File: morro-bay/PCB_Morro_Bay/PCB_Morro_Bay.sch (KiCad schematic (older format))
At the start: 84 parts, among them J1 POWER, J2 CAN, J23 POWER_OUT, J36 SWD, J37 GPIO, J38 USB_B, J39 ESERCOM, SW3 RESET, U1 MCP2515-xSO, U13 V7805-2000R, U2 SN65HVD232, U3 AZ1117-3.3, U4 ATSAMD21J18A-AU, Y1 8MHz, Y2 30MHz, Y3 32.768kHz

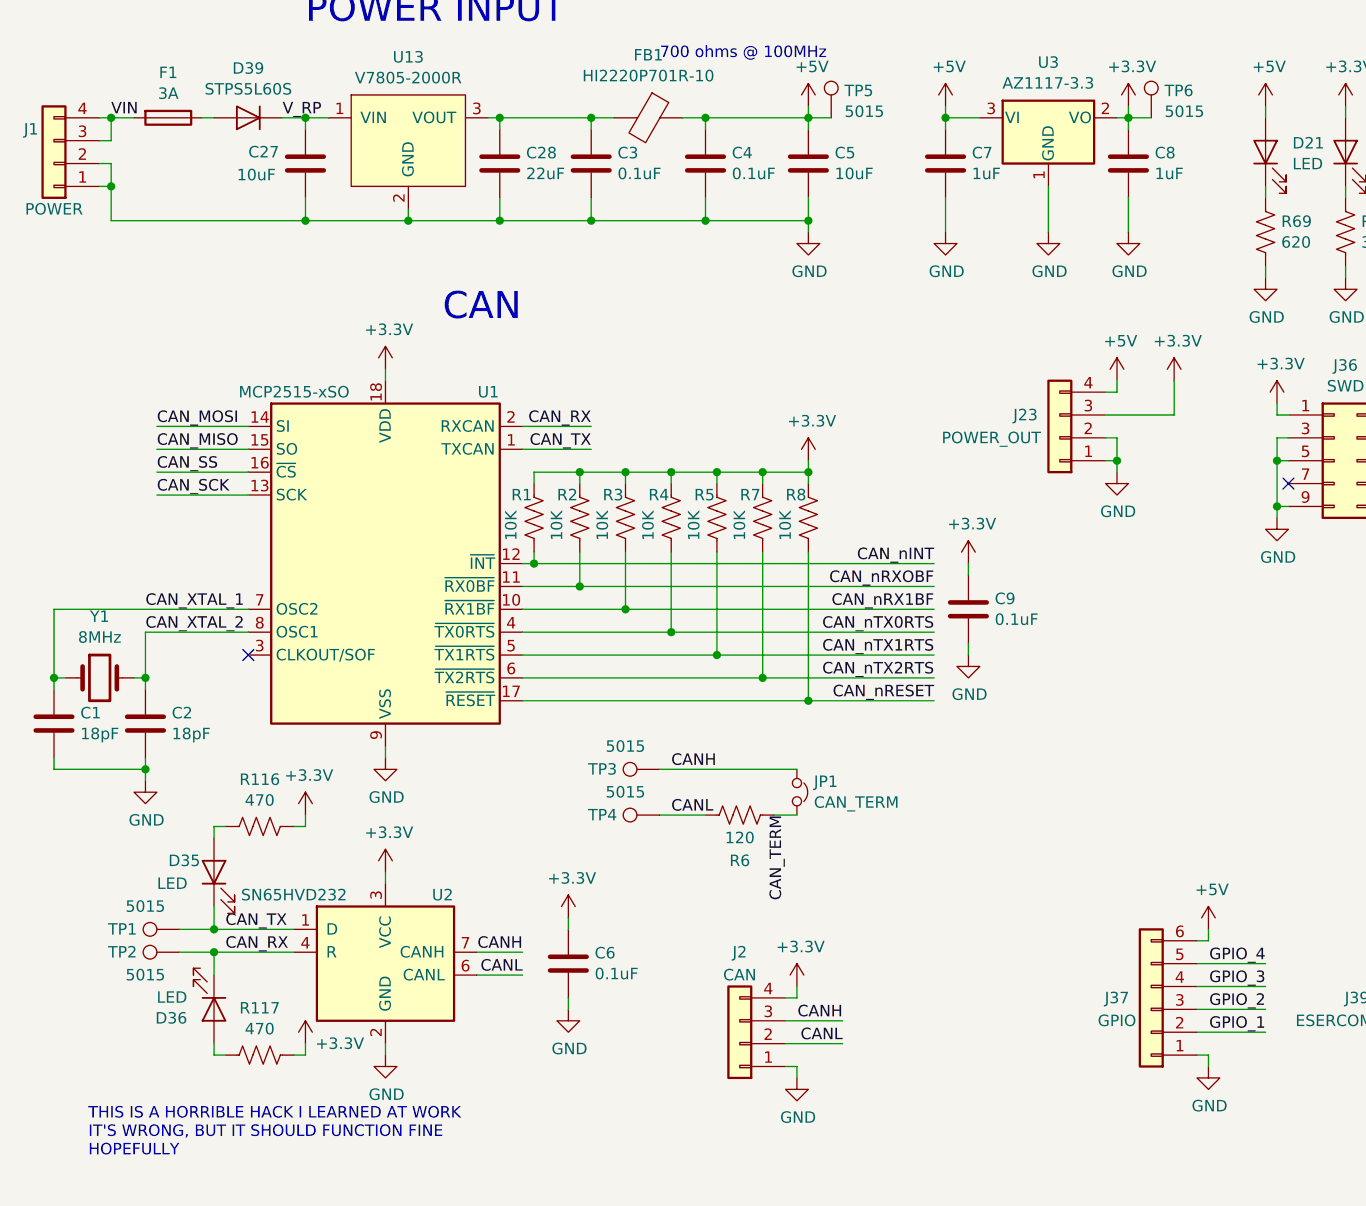
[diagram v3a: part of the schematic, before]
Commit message: Fix values of C7 and C8
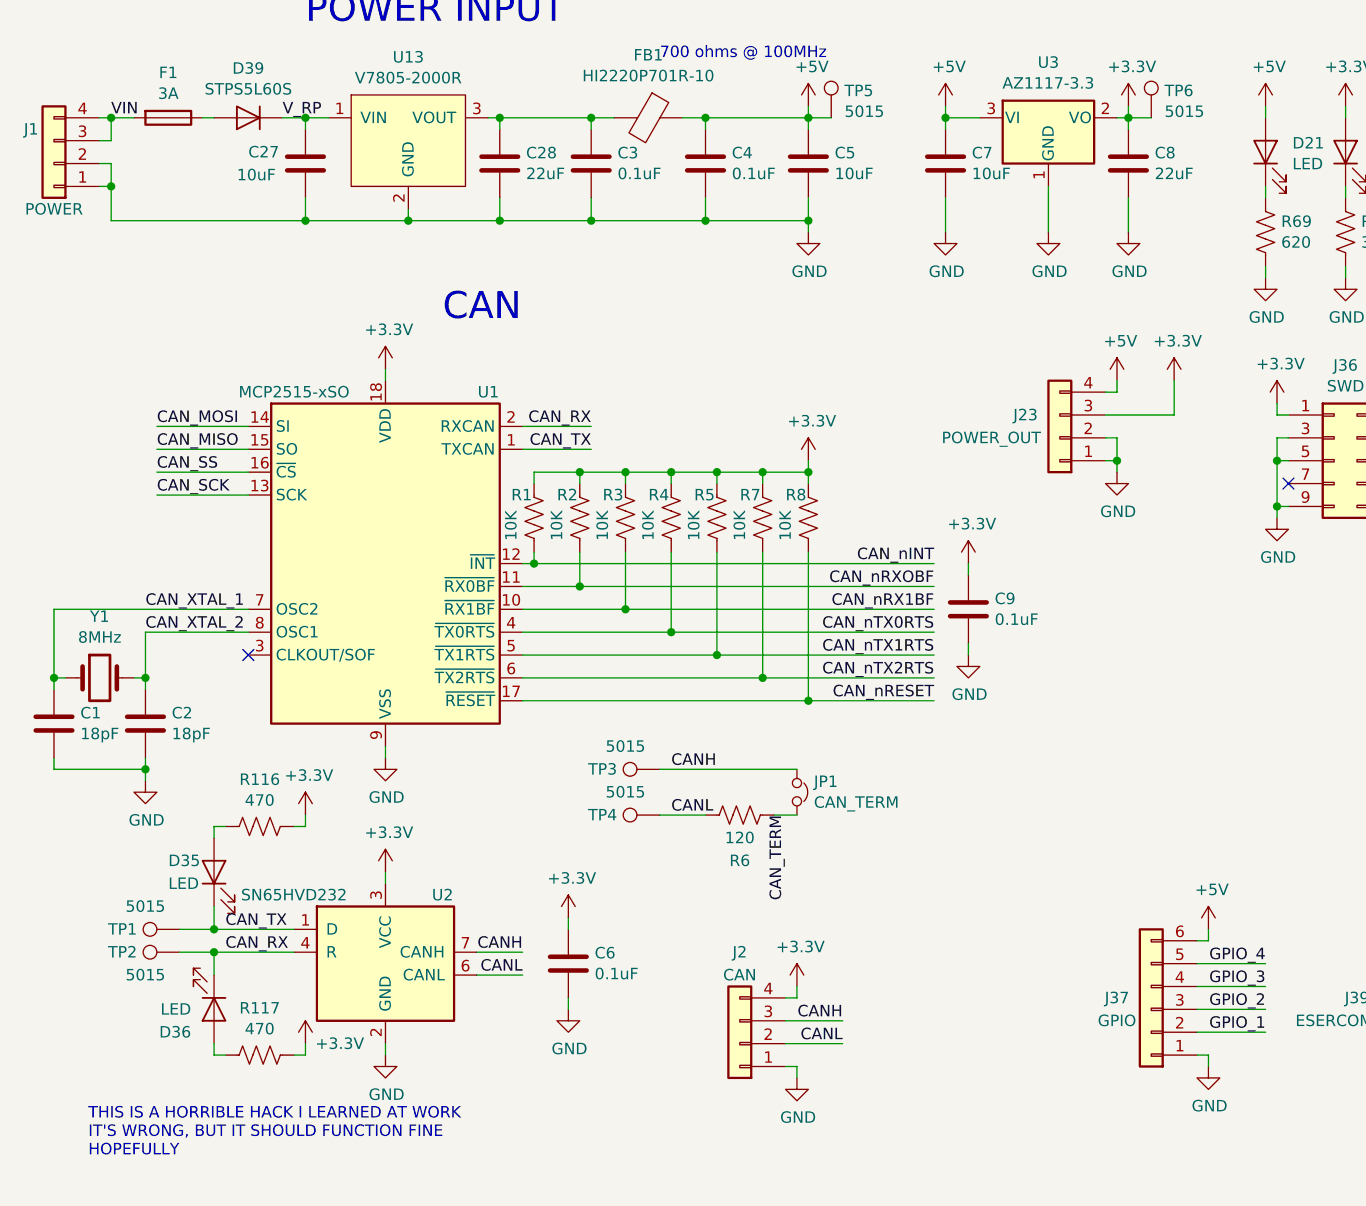
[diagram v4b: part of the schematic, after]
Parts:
- C7: value 1uF -> 10uF; Digikey https://www.digikey.ca/en/products/detail/samsung-electro-mechanics/CL10B105KA8NNNC/3886842 -> https://www.digikey.ca/en/products/detail/samsung-electro-mechanics/CL10A106MA8NRNC/3887527; Part Number CL10B105KA8NNNC -> CL10A106MA8NRNC
- C8: value 1uF -> 22uF; footprint Capacitor_SMD:C_0603_1608Metric_Pad1.05x0.95mm_HandSolder -> Capacitor_SMD:C_0805_2012Metric_Pad1.15x1.40mm_HandSolder; Digikey https://www.digikey.ca/en/products/detail/samsung-electro-m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 -> https://www.digikey.ca/product-detail/en/samsung-electro-me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; Part Number CL10B105KA8NNNC -> CL21A226MAQNNNE
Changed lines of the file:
@@
-$EndComp
-$Comp
-L Device:C C7
-U 1 1 5E3CE794
-P 4550 1350
-F 0 "C7" H 4665 1396 50  0000 L CNN
-F 1 "1uF" H 4665 1305 50  0000 L CNN
-F 2 "Capacitor_SMD:C_0603_1608Metric_Pad1.05x0.95mm_HandSolder" H 4588 1200 50  0001 C CNN
-F 3 "~" H 4550 1350 50  0001 C CNN
-F 4 "https://www.digikey.ca/en/products/detail/samsung-electro-mechanics/CL10B105KA8NNNC/3886842" H 4550 1350 50  0001 C CNN "Digikey"
-F 5 "CL10B105KA8NNNC" H 4550 1350 50  0001 C CNN "Part Number"
-	1    4550 1350
-	1    0    0    -1
 $EndComp
 $Comp
@@
 U 1 1 5ED157D8
 P 1350 5050
-F 0 "D36" V 1389 4933 50  0000 R CNN
-F 1 "LED" V 1298 4933 50  0000 R CNN
+F 0 "D36" V 1450 4950 50  0000 R CNN
+F 1 "LED" V 1350 4950 50  0000 R CNN
 F 2 "LED_SMD:LED_0603_1608Metric_Castellated" H 1350 5050 50  0001 C CNN
 F 3 "http://optoelectronics.liteon.com/upload/download/DS22-2000-222/LTST-C191KFKT.pdf" H 1350 5050 50  0001 C CNN
@@
 P 1350 4450
 F 0 "D35" V 1400 4650 50  0000 R CNN
-F 1 "LED" V 1300 4700 50  0000 R CNN
+F 1 "LED" V 1300 4650 50  0000 R CNN
 F 2 "LED_SMD:LED_0603_1608Metric_Castellated" H 1350 4450 50  0001 C CNN
 F 3 "http://optoelectronics.liteon.com/upload/download/DS22-2000-222/LTST-C191KFKT.pdf" H 1350 4450 50  0001 C CNN
@@
 $EndComp
 $Comp
-L Device:C C8
-U 1 1 5E7F39FA
-P 5350 1350
-F 0 "C8" H 5465 1396 50  0000 L CNN
-F 1 "1uF" H 5465 1305 50  0000 L CNN
-F 2 "Capacitor_SMD:C_0603_1608Metric_Pad1.05x0.95mm_HandSolder" H 5388 1200 50  0001 C CNN
-F 3 "~" H 5350 1350 50  0001 C CNN
-F 4 "https://www.digikey.ca/en/products/detail/samsung-electro-mechanics/CL10B105KA8NNNC/3886842" H 5350 1350 50  0001 C CNN "Digikey"
-F 5 "CL10B105KA8NNNC" H 5350 1350 50  0001 C CNN "Part Number"
-	1    5350 1350
-	1    0    0    -1
-$EndComp
-$Comp
 L Device:C C19
 U 1 1 5E80BB1C
@@
 	1    0    0    -1
 $EndComp
+$Comp
+L Device:C C7
+U 1 1 5E85940A
+P 4550 1350
+F 0 "C7" H 4665 1396 50  0000 L CNN
+F 1 "10uF" H 4665 1305 50  0000 L CNN
+F 2 "Capacitor_SMD:C_0603_1608Metric_Pad1.05x0.95mm_HandSolder" H 4588 1200 50  0001 C CNN
+F 3 "~" H 4550 1350 50  0001 C CNN
+F 4 "https://www.digikey.ca/en/products/detail/samsung-electro-mechanics/CL10A106MA8NRNC/3887527" H 4550 1350 50  0001 C CNN "Digikey"
+F 5 "CL10A106MA8NRNC	" H 4550 1350 50  0001 C CNN "Part Number"
+	1    4550 1350
+	1    0    0    -1
+$EndComp
+$Comp
+L Device:C C8
+U 1 1 5E88C625
+P 5350 1350
+AR Path="/5E88C625" Ref="C8"  Part="1"
+AR Path="/5E59A680/5E88C625" Ref="C?"  Part="1"
+F 0 "C8" H 5465 1396 50  0000 L CNN
+F 1 "22uF" H 5465 1305 50  0000 L CNN
+F 2 "Capacitor_SMD:C_0805_2012Metric_Pad1.15x1.40mm_HandSolder" H 5388 1200 50  0001 C CNN
+F 3 "~" H 5350 1350 50  0001 C CNN
+F 4 "CL21A226MAQNNNE" H 5350 1350 50  0001 C CNN "Part Number"
+F 5 "https://www.digikey.ca/product-detail/en/samsung-electro-mechanics/CL21A226MAQNNNE/1276-2908-1-ND/3890994" H 5350 1350 50  0001 C CNN "Digikey"
+	1    5350 1350
+	1    0    0    -1
+$EndComp

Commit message: Routing and layout work
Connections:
- net SAMD_ADC_1: now also U4.20 (PA11); no longer U4.61 (PB00)
- net SAMD_ADC_10: now also U4.11 (PB08); no longer U4.10 (PB07)
- net SAMD_ADC_11: now also U4.10 (PB07); no longer U4.11 (PB08)
- net SAMD_ADC_12: now also U4.9 (PB06); no longer U4.12 (PB09)
- net SAMD_ADC_13: now also U4.6 (PB05); no longer U4.13 (PA04)
- net SAMD_ADC_14: now also U4.5 (PB04); no longer U4.14 (PA05)
- net SAMD_ADC_15: now also U4.4 (PA03); no longer U4.15 (PA06)
- net SAMD_ADC_16: now also U4.3 (PA02); no longer U4.16 (PA07)
- net SAMD_ADC_17: now also U4.64 (PB03); no longer U4.17 (PA08)
- net SAMD_ADC_18: now also U4.63 (PB02); no longer U4.18 (PA09)
- net SAMD_ADC_19: now also U4.62 (PB01); no longer U4.19 (PA10)
- net SAMD_ADC_2: now also U4.19 (PA10); no longer U4.62 (PB01)
- net SAMD_ADC_20: now also U4.61 (PB00); no longer U4.20 (PA11)
- net SAMD_ADC_3: now also U4.18 (PA09); no longer U4.63 (PB02)
- net SAMD_ADC_4: now also U4.17 (PA08); no longer U4.64 (PB03)
- net SAMD_ADC_5: now also U4.16 (PA07); no longer U4.3 (PA02)
- net SAMD_ADC_6: now also U4.15 (PA06); no longer U4.4 (PA03)
- net SAMD_ADC_7: now also U4.14 (PA05); no longer U4.5 (PB04)
- net SAMD_ADC_8: now also U4.13 (PA04); no longer U4.6 (PB05)
- net SAMD_ADC_9: now also U4.12 (PB09); no longer U4.9 (PB06)
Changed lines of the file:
@@
 Text Notes 850  7300 0    118  ~ 0
 ANALOG INPUT
-Text GLabel 8700 2600 0    50   Input ~ 0
+Text GLabel 8700 2450 0    50   Input ~ 0
 SAMD_ADC_1
+Text GLabel 8700 2350 0    50   Input ~ 0
+SAMD_ADC_2
+Text GLabel 8700 2250 0    50   Input ~ 0
+SAMD_ADC_3
+Text GLabel 8700 2150 0    50   Input ~ 0
+SAMD_ADC_4
+Text GLabel 8700 2050 0    50   Input ~ 0
+SAMD_ADC_5
+Text GLabel 8700 1950 0    50   Input ~ 0
+SAMD_ADC_6
+Text GLabel 8700 1850 0    50   Input ~ 0
+SAMD_ADC_7
+Text GLabel 8700 1750 0    50   Input ~ 0
+SAMD_ADC_8
+Text GLabel 8700 3500 0    50   Input ~ 0
+SAMD_ADC_9
+Text GLabel 8700 3400 0    50   Input ~ 0
+SAMD_ADC_10
+Text GLabel 8700 3300 0    50   Input ~ 0
+SAMD_ADC_11
+Text GLabel 8700 3200 0    50   Input ~ 0
+SAMD_ADC_12
+Text GLabel 8700 3100 0    50   Input ~ 0
+SAMD_ADC_13
+Text GLabel 8700 3000 0    50   Input ~ 0
+SAMD_ADC_14
+Text GLabel 8700 1650 0    50   Input ~ 0
+SAMD_ADC_15
+Text GLabel 8700 1550 0    50   Input ~ 0
+SAMD_ADC_16
+Text GLabel 8700 2900 0    50   Input ~ 0
+SAMD_ADC_17
+Text GLabel 8700 2800 0    50   Input ~ 0
+SAMD_ADC_18
 Text GLabel 8700 2700 0    50   Input ~ 0
-SAMD_ADC_2
-Text GLabel 8700 2800 0    50   Input ~ 0
-SAMD_ADC_3
-Text GLabel 8700 2900 0    50   Input ~ 0
-SAMD_ADC_4
-Text GLabel 8700 1550 0    50   Input ~ 0
-SAMD_ADC_5
-Text GLabel 8700 1650 0    50   Input ~ 0
-SAMD_ADC_6
-Text GLabel 8700 3000 0    50   Input ~ 0
-SAMD_ADC_7
-Text GLabel 8700 3100 0    50   Input ~ 0
-SAMD_ADC_8
-Text GLabel 8700 3200 0    50   Input ~ 0
-SAMD_ADC_9
-Text GLabel 8700 3300 0    50   Input ~ 0
-SAMD_ADC_10
-Text GLabel 8700 3400 0    50   Input ~ 0
-SAMD_ADC_11
-Text GLabel 8700 3500 0    50   Input ~ 0
-SAMD_ADC_12
-Text GLabel 8700 1750 0    50   Input ~ 0
-SAMD_ADC_13
-Text GLabel 8700 1850 0    50   Input ~ 0
-SAMD_ADC_14
-Text GLabel 8700 1950 0    50   Input ~ 0
-SAMD_ADC_15
-Text GLabel 8700 2050 0    50   Input ~ 0
-SAMD_ADC_16
-Text GLabel 8700 2150 0    50   Input ~ 0
-SAMD_ADC_17
-Text GLabel 8700 2250 0    50   Input ~ 0
-SAMD_ADC_18
-Text GLabel 8700 2350 0    50   Input ~ 0
 SAMD_ADC_19
 Wire Wire Line
@@
 Wire Wire Line
 	2700 3100 2750 3100
-Text GLabel 8700 2450 0    50   Input ~ 0
+Text GLabel 8700 2600 0    50   Input ~ 0
 SAMD_ADC_20
 Wire Wire Line

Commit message: Routing
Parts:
- R120, R121, R122, R123: value 0 -> DNP
- Y3: footprint Crystal:Crystal_SMD_SeikoEpson_MC146-4Pin_6.7x1.5mm_HandSoldering -> PCB_Morro_Bay:Crystal_Epson_MC-146
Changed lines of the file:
@@
 F 0 "Y3" H 7700 1668 50  0000 C CNN
 F 1 "32.768kHz" H 7700 1577 50  0000 C CNN
-F 2 "Crystal:Crystal_SMD_SeikoEpson_MC146-4Pin_6.7x1.5mm_HandSoldering" H 7700 1400 50  0001 C CNN
+F 2 "PCB_Morro_Bay:Crystal_Epson_MC-146" H 7700 1400 50  0001 C CNN
 F 3 "https://support.epson.biz/td/api/doc_check.php?dl=brief_MC-146&lang=en" H 7700 1400 50  0001 C CNN
 F 4 "https://www.digikey.ca/product-detail/en/epson/MC-146-32-7680KA-AC0-ROHS/SER4303CT-ND/7932290" H 7700 1400 50  0001 C CNN "Digikey"
@@
 P 5000 7150
 F 0 "R120" H 5068 7196 50  0000 L CNN
-F 1 "0" H 5068 7105 50  0000 L CNN
+F 1 "DNP" H 5068 7105 50  0000 L CNN
 F 2 "Resistor_SMD:R_0805_2012Metric_Pad1.15x1.40mm_HandSolder" V 5040 7140 50  0001 C CNN
 F 3 "~" H 5000 7150 50  0001 C CNN
@@
 P 5300 7150
 F 0 "R121" H 5368 7196 50  0000 L CNN
-F 1 "0" H 5368 7105 50  0000 L CNN
+F 1 "DNP" H 5368 7105 50  0000 L CNN
 F 2 "Resistor_SMD:R_0805_2012Metric_Pad1.15x1.40mm_HandSolder" V 5340 7140 50  0001 C CNN
 F 3 "~" H 5300 7150 50  0001 C CNN
@@
 P 5600 7150
 F 0 "R122" H 5668 7196 50  0000 L CNN
-F 1 "0" H 5668 7105 50  0000 L CNN
+F 1 "DNP" H 5668 7105 50  0000 L CNN
 F 2 "Resistor_SMD:R_0805_2012Metric_Pad1.15x1.40mm_HandSolder" V 5640 7140 50  0001 C CNN
 F 3 "~" H 5600 7150 50  0001 C CNN
@@
 P 5900 7150
 F 0 "R123" H 5968 7196 50  0000 L CNN
-F 1 "0" H 5968 7105 50  0000 L CNN
+F 1 "DNP" H 5968 7105 50  0000 L CNN
 F 2 "Resistor_SMD:R_0805_2012Metric_Pad1.15x1.40mm_HandSolder" V 5940 7140 50  0001 C CNN
 F 3 "~" H 5900 7150 50  0001 C CNN

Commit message: Add missing part values
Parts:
- J23: Digikey (none) -> https://www.digikey.ca/products/en?keywords=430450400; Part Number (none) -> 0430450400
- U1: Digikey (none) -> https://www.digikey.ca/product-detail/en/microchip-technolo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; Part Number (none) -> MCP2515T-I/SO
- U2: Digikey (none) -> https://www.digikey.ca/product-detail/en/texas-instruments/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; Part Number (none) -> SN65HVD232DR
- U4: Digikey (none) -> https://www.digikey.ca/products/en/integrated-circuits-ics/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; Part Number (none) -> ATSAMD21J18A-AUT
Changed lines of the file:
@@
 F 2 "Package_SO:SOIC-18W_7.5x11.6mm_P1.27mm" H 2100 2200 50  0001 C CIN
 F 3 "http://ww1.microchip.com/downloads/en/DeviceDoc/MCP2515-Stand-Alone-CAN-Controller-with-SPI-20001801J.pdf" H 2200 2300 50  0001 C CNN
+F 4 "https://www.digikey.ca/product-detail/en/microchip-technology/MCP2515T-I-SO/MCP2515T-I-SOCT-ND/4307902" H 2100 3100 50  0001 C CNN "Digikey"
+F 5 "MCP2515T-I/SO" H 2100 3100 50  0001 C CNN "Part Number"
 	1    2100 3100
 	1    0    0    -1
@@
 F 2 "Package_QFP:TQFP-64_10x10mm_P0.5mm" H 9650 3150 50  0001 C CNN
 F 3 "http://ww1.microchip.com/downloads/en/DeviceDoc/SAM_D21_DA1_Family_Data%20Sheet_DS40001882E.pdf" H 9650 3150 50  0001 C CNN
+F 4 "https://www.digikey.ca/products/en/integrated-circuits-ics/embedded-microcontrollers/685?k=ATSAMD21J18A-AU&k=&pkeyword=ATSAMD21J18A-AU&sv=0&pv7=2&sf=0&quantity=&ColumnSort=0&page=1&pageSize=25" H 9500 2450 50  0001 C CNN "Digikey"
+F 5 "ATSAMD21J18A-AUT" H 9500 2450 50  0001 C CNN "Part Number"
 	1    9500 2450
 	1    0    0    -1
@@
 F 2 "Package_SO:SOIC-8_3.9x4.9mm_P1.27mm" H 2100 4300 50  0001 C CNN
 F 3 "http://www.ti.com/lit/ds/symlink/sn65hvd230.pdf" H 2000 5200 50  0001 C CNN
+F 4 "https://www.digikey.ca/product-detail/en/texas-instruments/SN65HVD232DR/296-26344-1-ND/2254978" H 2100 4800 50  0001 C CNN "Digikey"
+F 5 "SN65HVD232DR" H 2100 4800 50  0001 C CNN "Part Number"
 	1    2100 4800
 	1    0    0    -1
@@
 F 1 "POWER_OUT" H 5350 2550 50  0000 C CNN
 F 2 "Connector_Molex:Molex_Micro-Fit_3.0_43045-0400_2x02_P3.00mm_Horizontal" H 5050 2550 50  0001 C CNN
-F 3 "~" H 5050 2550 50  0001 C CNN
+F 3 "https://www.molex.com/pdm_docs/sd/430450400_sd.pdf" H 5050 2550 50  0001 C CNN
+F 4 "https://www.digikey.ca/products/en?keywords=430450400" H 5050 2550 50  0001 C CNN "Digikey"
+F 5 "0430450400" H 5050 2550 50  0001 C CNN "Part Number"
 	1    5050 2550
 	-1   0    0    1
